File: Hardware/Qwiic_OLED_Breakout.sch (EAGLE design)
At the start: 29 parts, among them J1 QWIIC_RIGHT_ANGLE, J2 QWIIC_RIGHT_ANGLE

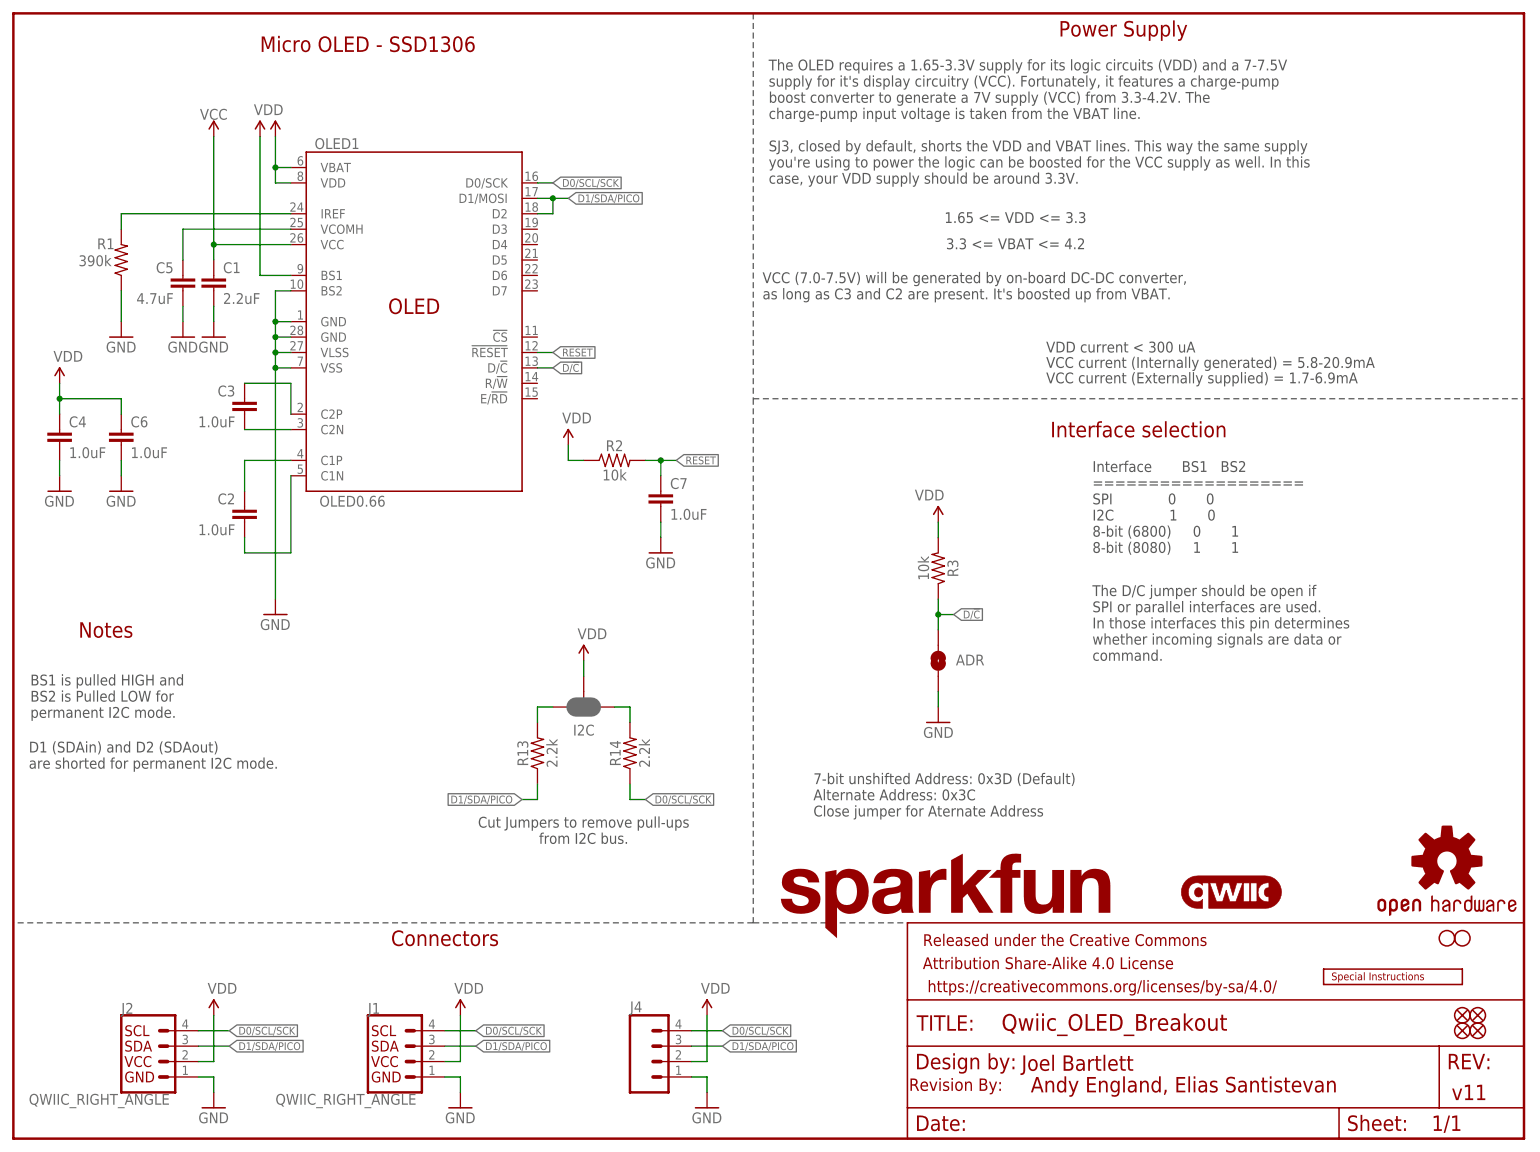
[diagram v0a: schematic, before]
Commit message: Moves Ordering Instructions
* Updates notes in schematics
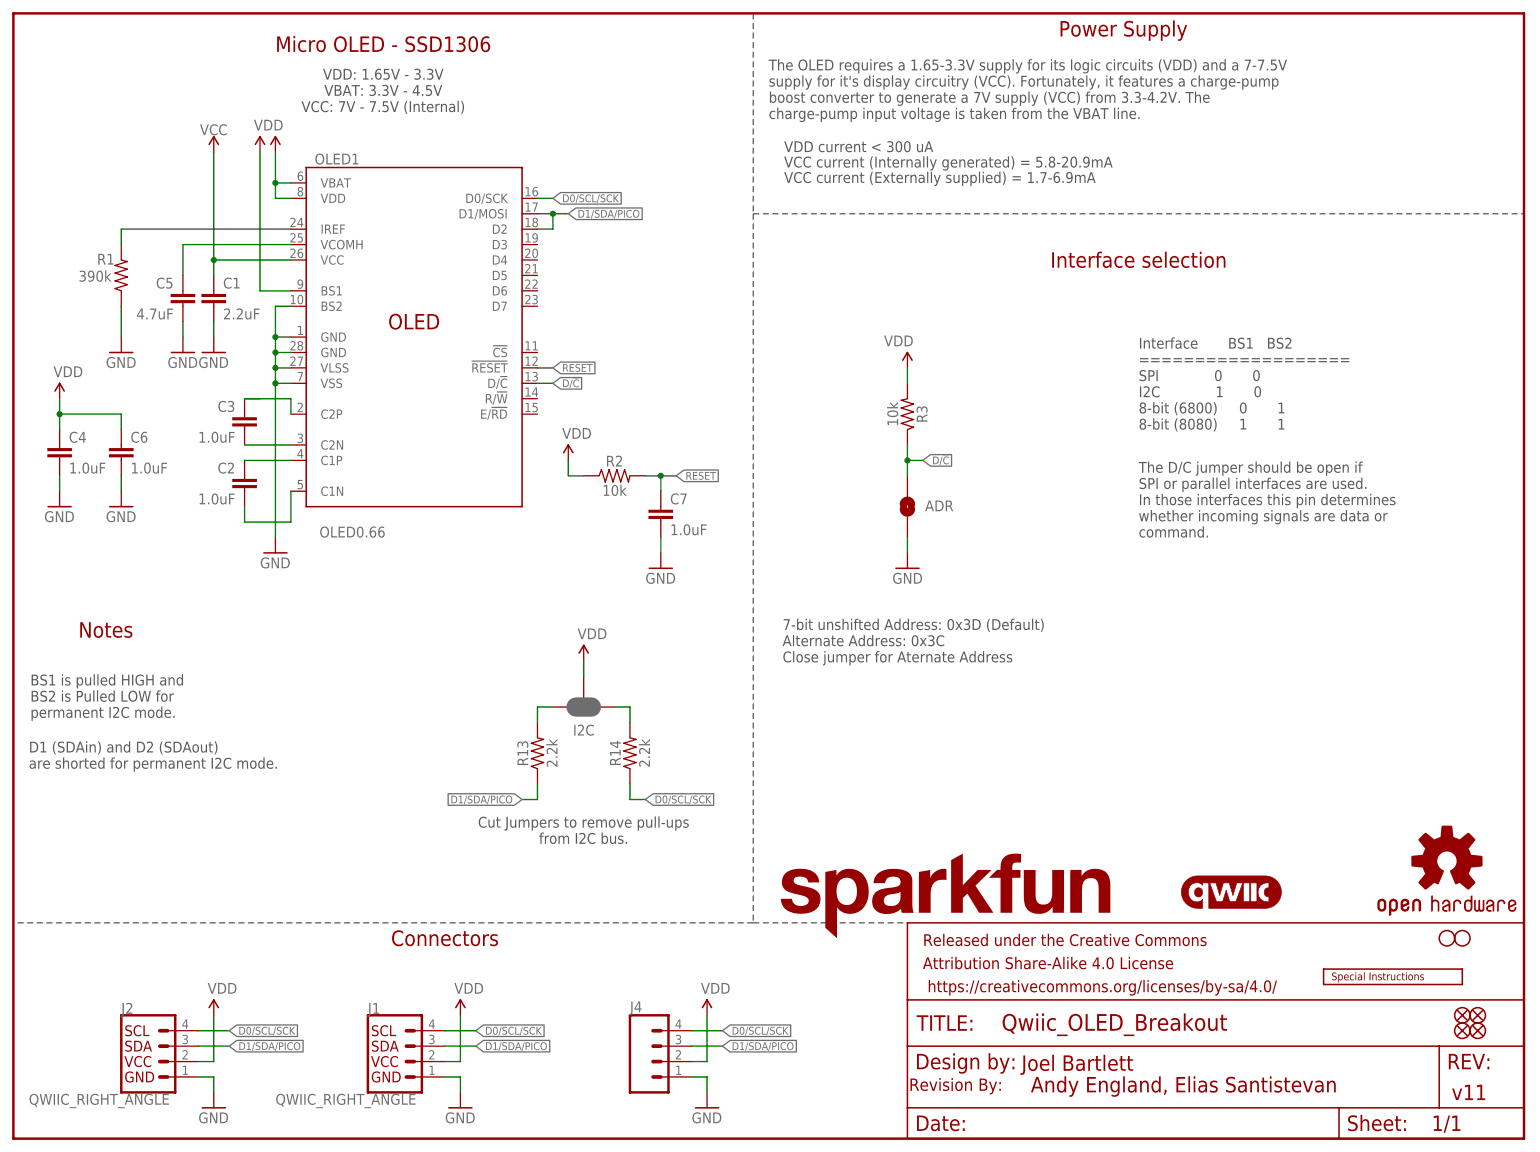
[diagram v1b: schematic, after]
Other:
- note added: "The OLED requires a 1.65-3.3V supply for its logic circuits (VDD) and a 7-7.5V supply for it's display circuitry (VCC). Fortunately, it features a charge-pump boost converter to generate a 7V supply (VCC) from 3.3-4.2V. The charge-pump input voltage is taken from the VBAT line."
- note added: "VDD: 1.65V - 3.3V VBAT: 3.3V - 4.5V VCC: 7V - 7.5V (Internal)"
- note removed: "1.65 <= VDD <= 3.3"
- note removed: "3.3 <= VBAT <= 4.2"
- note removed: "The OLED requires a 1.65-3.3V supply for its logic circuits (VDD) and a 7-7.5V supply for it's display circuitry (VCC). Fortunately, it features a charge-pump boost converter to generate a 7V supply (VCC) from 3.3-4.2V. The charge-pump input voltage is taken from the VBAT line. SJ3, closed by default, shorts the VDD and VBAT lines. This way the same supply you're using to power the logic can be b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"
- note removed: "VCC (7.0-7.5V) will be generated by on-board DC-DC converter, as long as C3 and C2 are present. It's boosted up from VBAT."
- moved on the sheet: ADR, C1, C2, C3, C4, C5, C6, C7, OLED1, R1, R2, R3

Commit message: Adds a single via
* Gets judicious with the text in the schematic
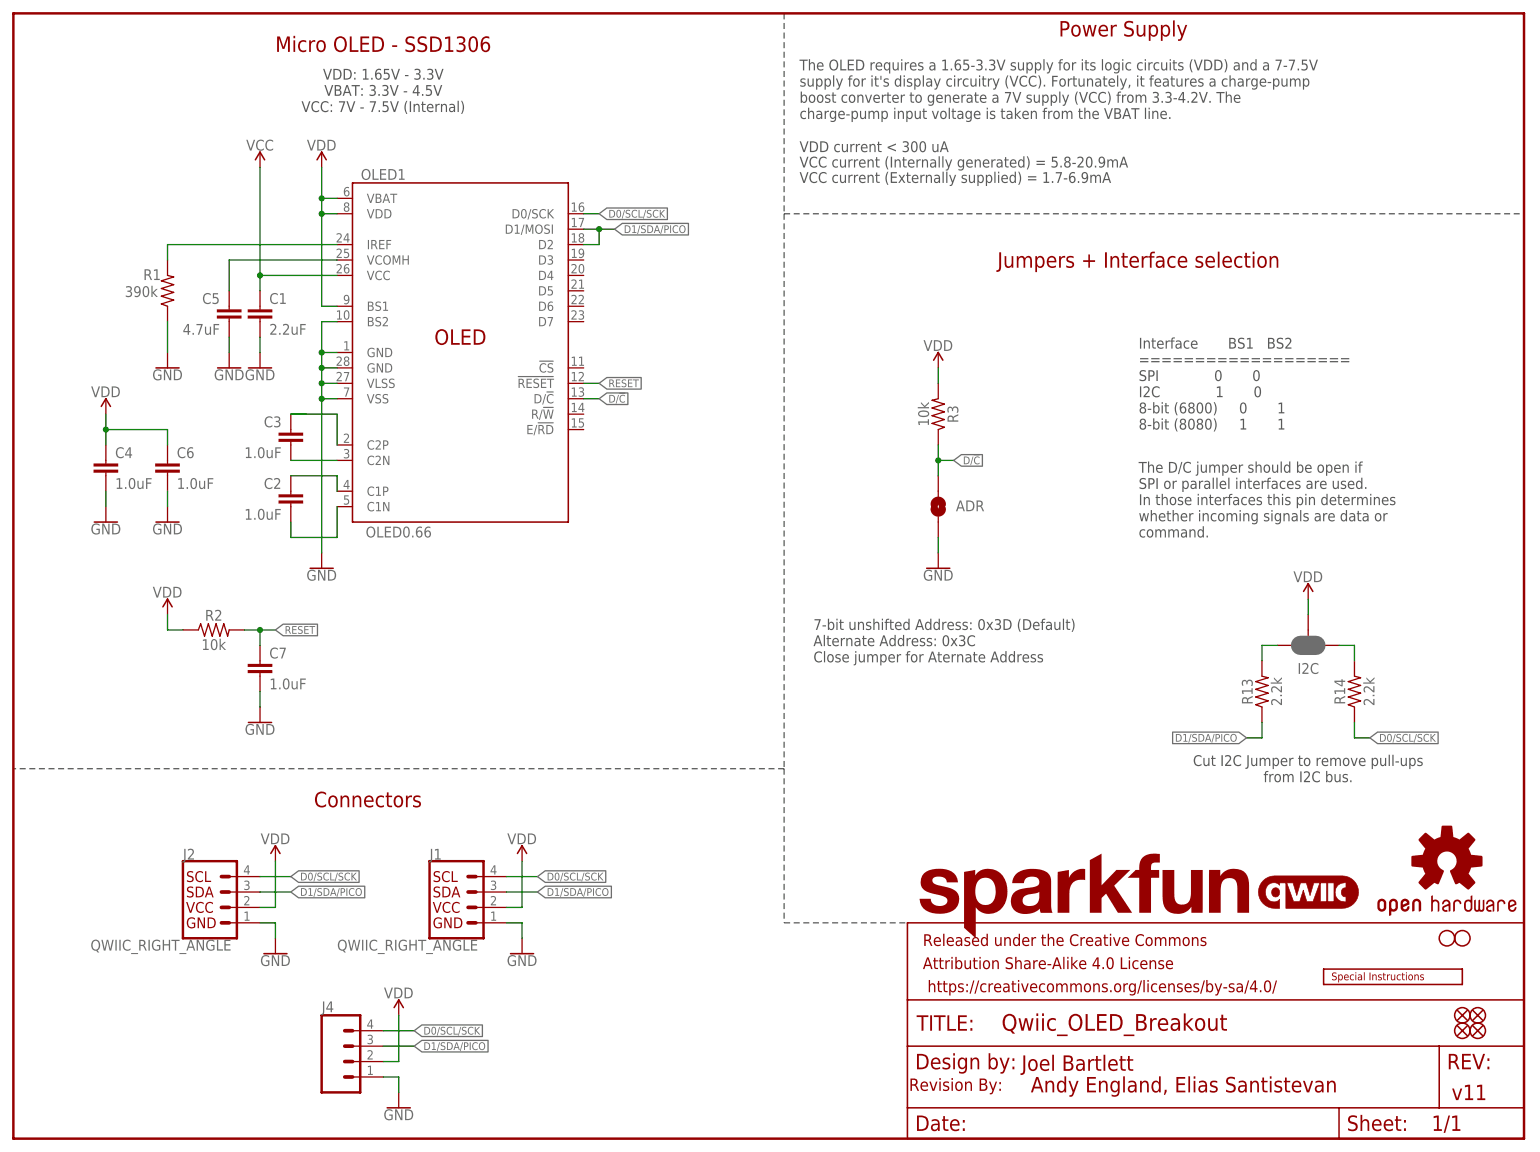
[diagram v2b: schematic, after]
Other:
- note added: "Cut I2C Jumper to remove pull-ups from I2C bus."
- note added: "Jumpers + Interface selection"
- note removed: "BS1 is pulled HIGH and BS2 is Pulled LOW for permanent I2C mode."
- note removed: "Cut Jumpers to remove pull-ups from I2C bus."
- note removed: "D1 (SDAin) and D2 (SDAout) are shorted for permanent I2C mode."
- note removed: "Interface selection"
- note removed: "Notes"
- moved on the sheet: ADR, C1, C2, C3, C4, C5, C6, C7, I2C, J1, J2, J4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

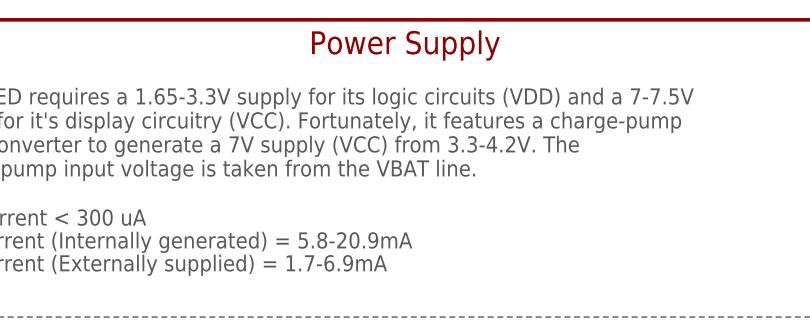
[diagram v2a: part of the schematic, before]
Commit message: Adds new panel after bringing the tabbed part to match the panel
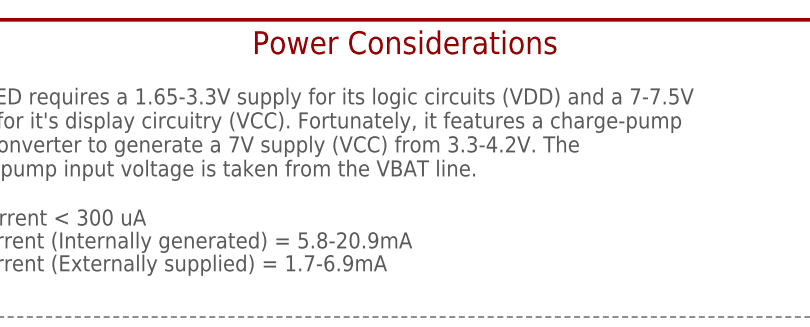
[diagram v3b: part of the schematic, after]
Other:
- note added: "Power Considerations"
- note removed: "Power Supply"
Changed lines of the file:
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@@
 </text>
 <text x="223.52" y="38.1" size="1.778" layer="97"></text>
-<text x="182.88" y="182.88" size="2.54" layer="94" font="vector" align="center">Power Supply</text>
+<text x="182.88" y="182.88" size="2.54" layer="94" font="vector" align="center">Power Considerations</text>
 <text x="129.54" y="177.8" size="1.778" layer="97" font="vector" align="top-left">The OLED requires a 1.65-3.3V supply for its logic circuits (VDD) and a 7-7.5V
 supply for it's display circuitry (VCC). Fortunately, it features a charge-pump
